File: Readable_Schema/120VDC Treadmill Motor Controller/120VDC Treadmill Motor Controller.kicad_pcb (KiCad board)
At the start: 4 copper layers, 186.8 x 133.2 mm, 141 parts, among them J1 TB005-762-03BE, J2 OSTT7020150, J3 TB0011-350-08BE, J4 TB0011-350-08BE, J5 TB0011-350-08BE, J6 TB0011-350-03BE, J7 OSTT7020150, J9 OSTT7020150, K1 T9GV1L14-24, Q1 IPP200N25N3 G, Q2 IPP200N25N3 G, Q3 IPP200N25N3 G, Q4 IPP200N25N3 G, Q5 IPP60R060P7XKSA1, Q7 DN2450N8-G, Q8 VOM1271T, U1 UCC21530DWKR, U2 UCC21530DWKR, U3 TMCS1126B42QDVGRQ1, U4 SN74HCS08DYYR, U5 TPSI3050QDWZRQ1, U6 AMC1311BDWVR

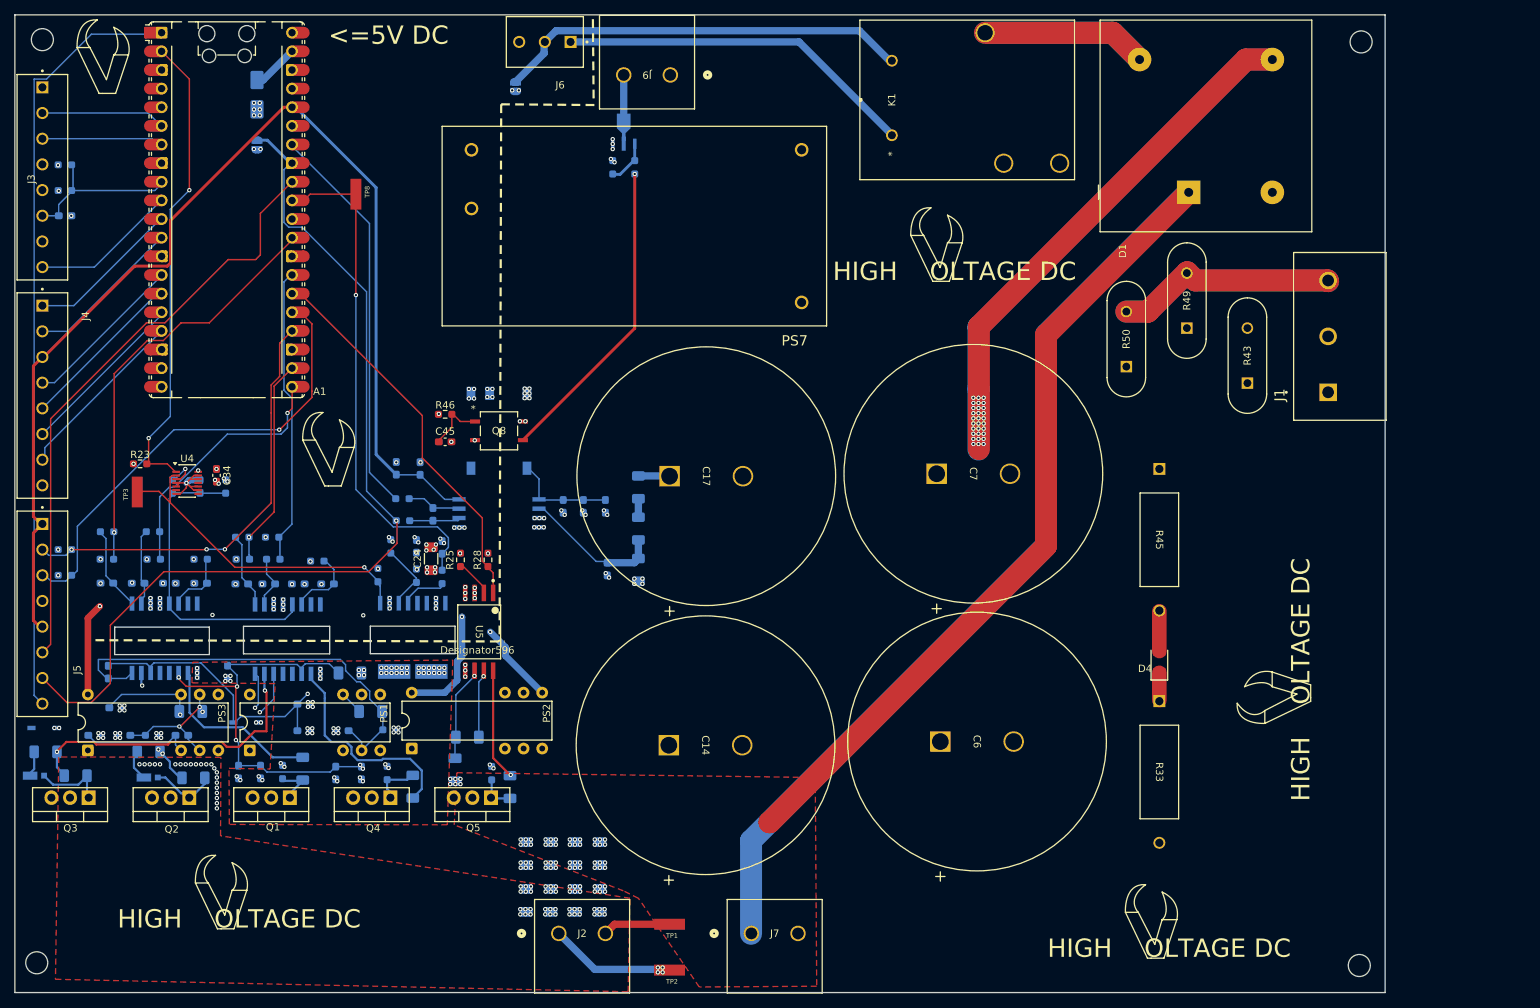
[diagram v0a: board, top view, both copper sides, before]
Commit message: -Finished going back and adding some valuable test points. -Realized that 2oz inner copper layer thickness costs way too much so looking at getting 1oz instead. --Need to double check that my pour sizes and inside traces are sized appropiately for 1oz. Not sure how to check
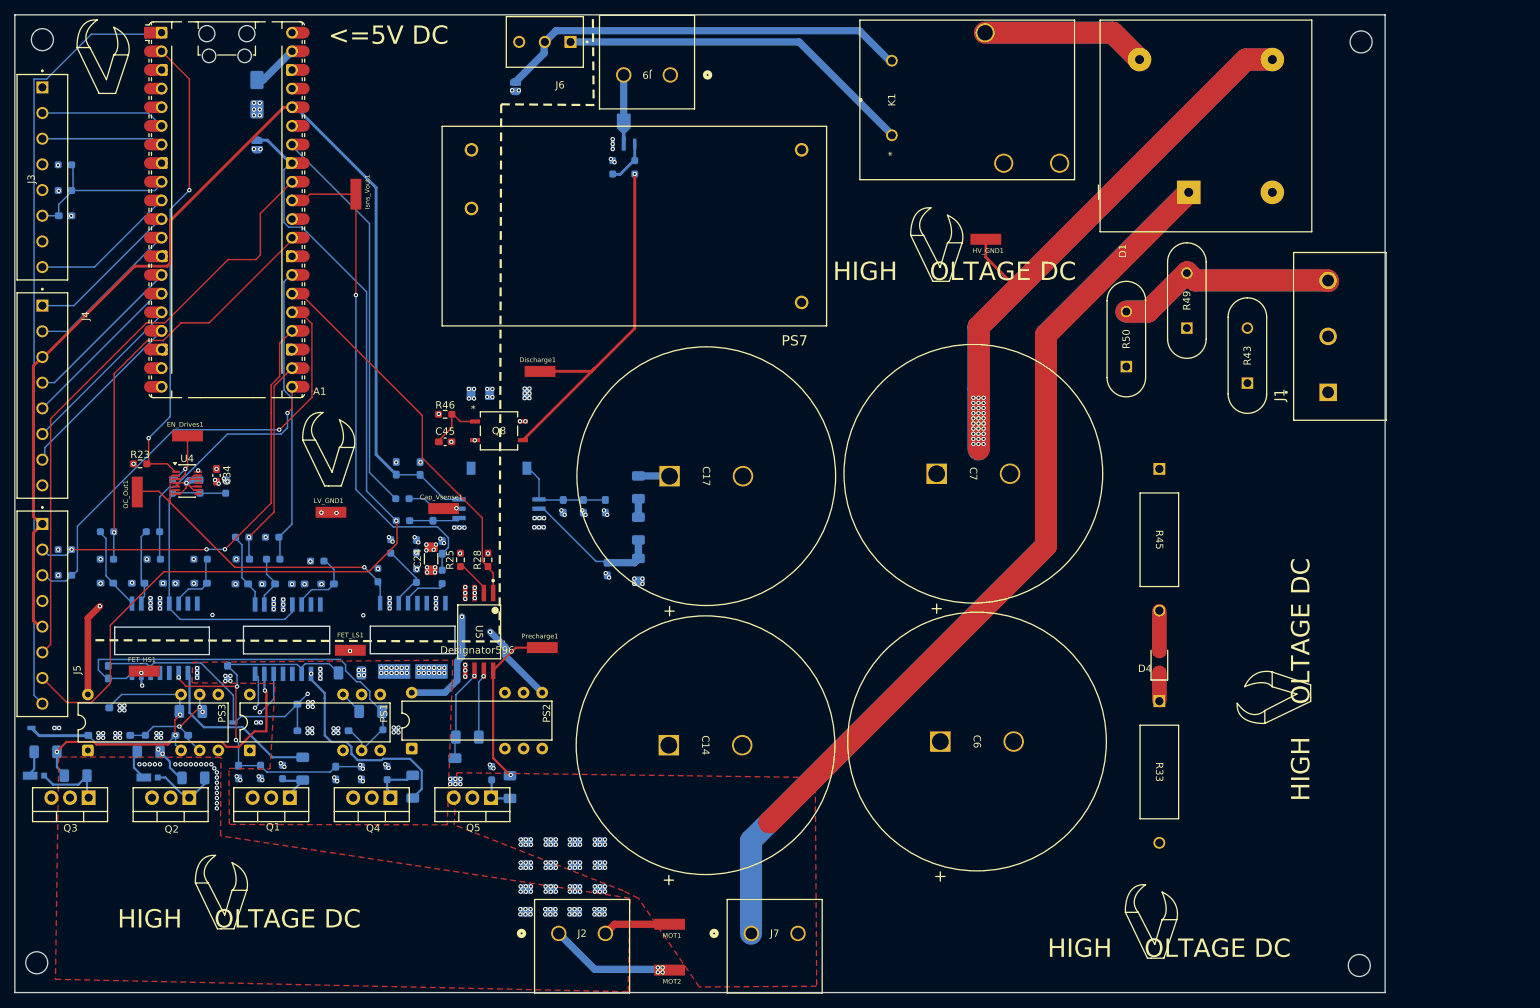
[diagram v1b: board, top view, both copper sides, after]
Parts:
- added Cap_Vsense1: RCWCTE, Treadmill_Feet:RCWCTE, F.Cu at (75.0, 113.1)
- added Discharge1: RCWCTE, Treadmill_Feet:RCWCTE, F.Cu at (88.1, 94.4)
- added EN_Drives1: RCWCTE, Treadmill_Feet:RCWCTE, F.Cu at (40.0, 103.2)
- added FET_HS1: RCWCTE, Treadmill_Feet:RCWCTE, F.Cu at (34.1, 135.2)
- added FET_LS1: RCWCTE, Treadmill_Feet:RCWCTE, F.Cu at (62.2, 132.4)
- added HV_GND1: RCWCTE, Treadmill_Feet:RCWCTE, F.Cu at (148.8, 76.4)
- added LV_GND1: RCWCTE, Treadmill_Feet:RCWCTE, F.Cu at (59.6, 113.6)
- added Precharge1: RCWCTE, Treadmill_Feet:RCWCTE, F.Cu at (88.4, 132.1)
- Q5: value IPP60R060P7XKSA1 -> IPP200N25N3 G
- renumbered TP8 to Isns_Vout1, TP1 to MOT1, TP2 to MOT2, TP3 to OC_Out1
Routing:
- net /H_Bridge/hs_ps_2_-: track 45.0 -> 56.1 mm, vias 2 -> 3
- net HV_GND: track 143.6 -> 152.1 mm
- net Net-(U5-VDRV): track 15.3 -> 23.3 mm
- net Net-(Discharge1-Pad1): track 42.6 -> 50.2 mm
- net Net-(U1-OUTB): track 28.6 -> 35.4 mm, vias 0 -> 2
- net /Feedback/EN_Drives: track 4.30 -> 8.88 mm
- net Net-(U6-VOUTP): vias 0 -> 1
- net Net-(U2-OUTA): vias 3 -> 4
- net LV_GND: vias 64 -> 66

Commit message: -Realizing we can only afford 1oz copper on all 4 layers, trying to rework some of the traces and board fills accordingly. -Moved the smaller caps feeding the top of the H bridge directly in front of the mosfets they're feeding (duh) -Made no effort to reduce crossing signal lines from the gate drives. I think this would probably require a board redesign? -May need to ask the question of whether it may be worth trying to compress thing to reach the next minimum board size
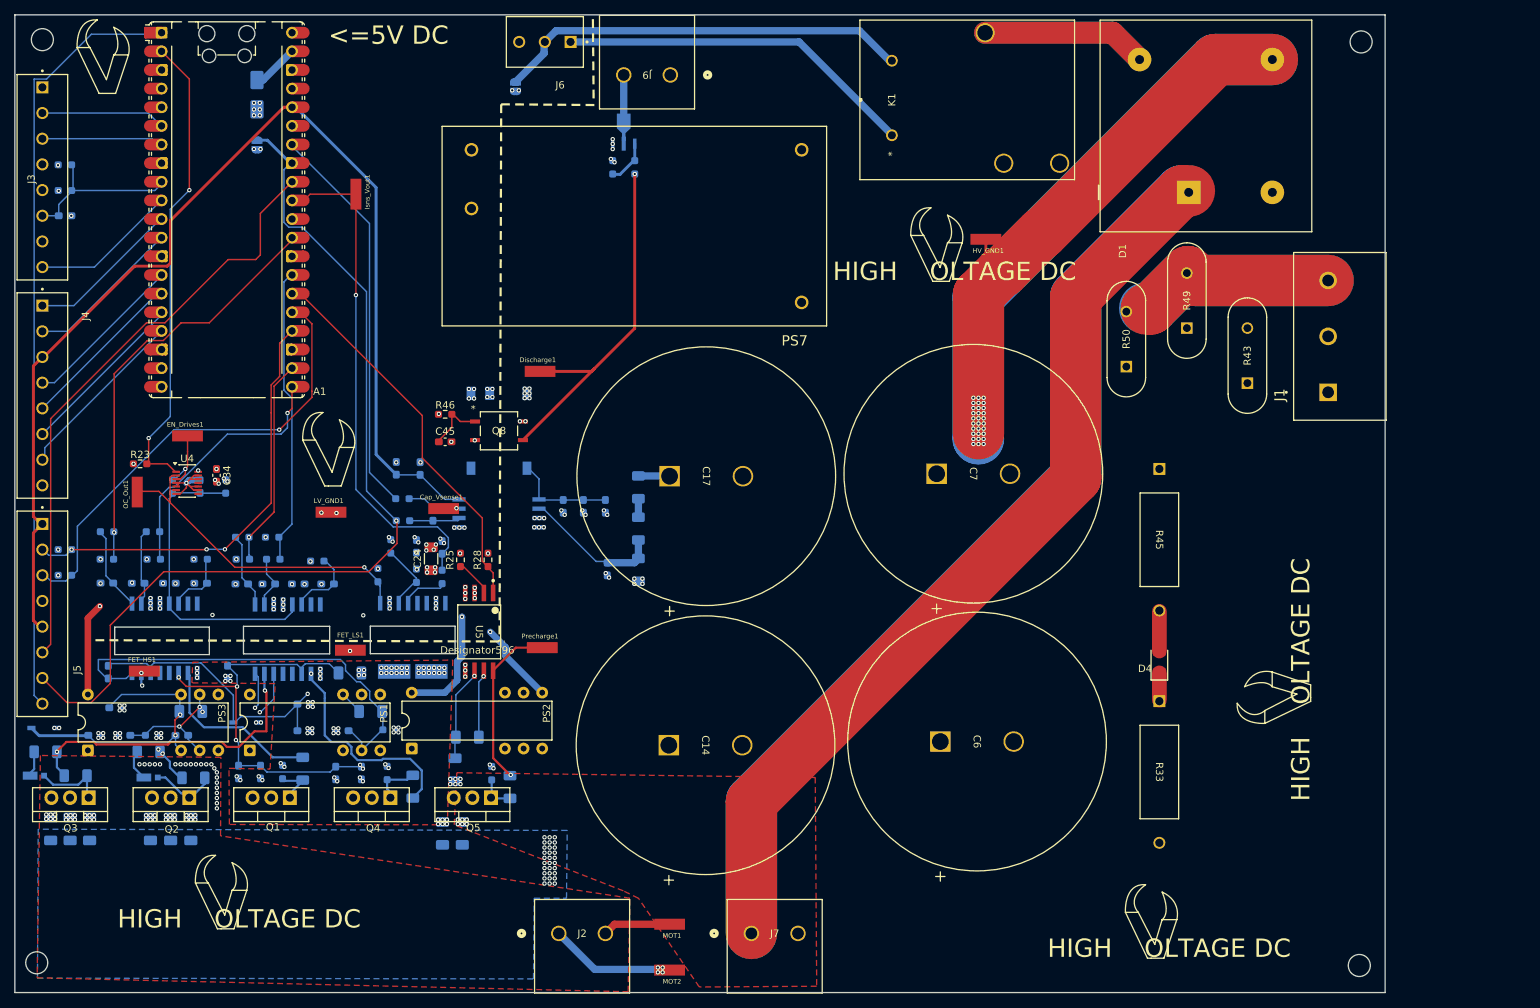
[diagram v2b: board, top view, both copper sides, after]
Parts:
- moved C50 72.9 mm to (24.1, 156.8)
- moved C49 72.2 mm to (21.4, 156.8)
- moved C28 60.3 mm to (26.7, 156.8)
- moved C51 58.6 mm to (37.8, 156.8), turned to -90 degrees
- moved C32 55.4 mm to (35.0, 156.8)
- moved C52 52.5 mm to (40.5, 156.8), turned to -90 degrees
- moved C53 12.4 mm to (77.5, 157.4), turned to -90 degrees
- moved C54 11.7 mm to (74.8, 157.4), turned to -90 degrees
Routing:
- net Net-(D1-+): track 235.3 -> 253.0 mm
- net Net-(J1-Pin_3): track 60.4 -> 55.2 mm
- net HV_GND: track 152.1 -> 153.6 mm, vias 129 -> 111
- added copper zone on B.Cu, net HV_GND

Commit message: For cost reasons we want all 1oz copper layers. This means --Inner copper for 20C rise at 1oz = 33mm min width of either trace or board fills --Outer copper for 20C rise at 1oz = 12mm min width of either trace or board fills
The conjestion near the fets makes this challenging
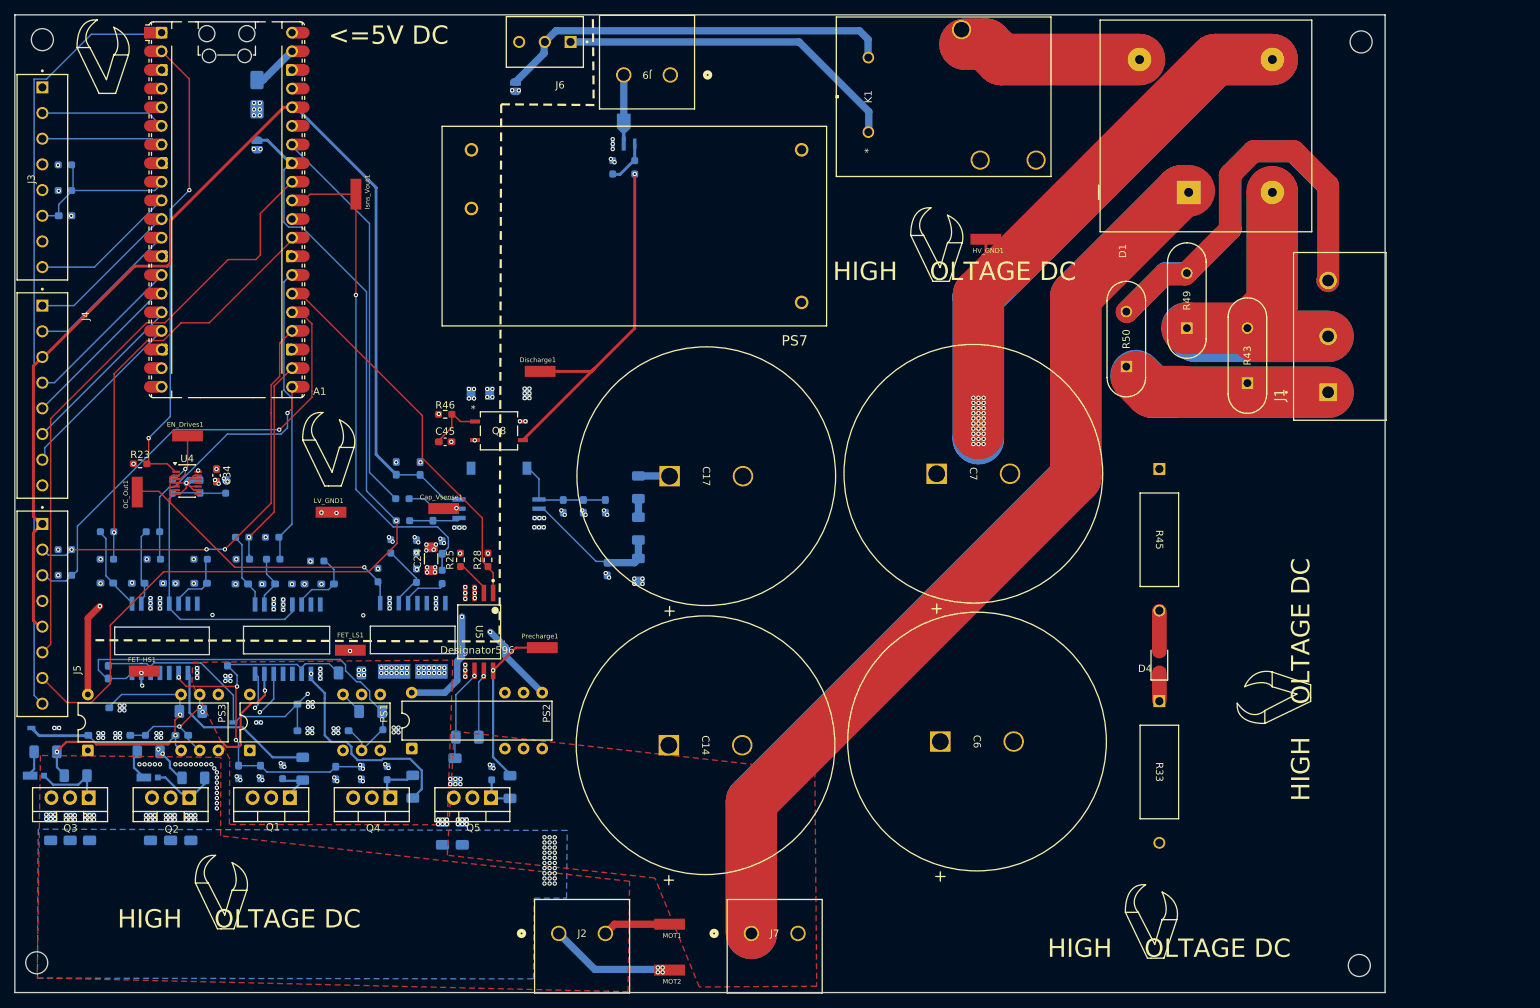
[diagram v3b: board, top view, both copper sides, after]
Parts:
- moved K1 3.24 mm to (132.8, 61.8)
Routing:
- net /Power/N: track 0.00 -> 134.4 mm
- net Net-(J1-Pin_3): track 55.2 -> 111.8 mm
- net /Power/L: track 0.00 -> 54.2 mm
- net Net-(D1-Pad2): track 45.1 -> 49.3 mm
- net Net-(J6-Pin_2): track 56.2 -> 54.2 mm
- net Net-(J6-Pin_1): track 49.1 -> 47.3 mm
- net Net-(U1-OUTA): track 41.9 -> 41.2 mm
- net Net-(U5-VDRV): track 23.3 -> 22.7 mm
- added copper zone on In1.Cu, net /Power/L
- removed copper zone on In1.Cu, net /Power/N

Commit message: -Started to move the Current sense off to the side on the board due to limited space for these massive traces and what not. This entails quite a few random moves
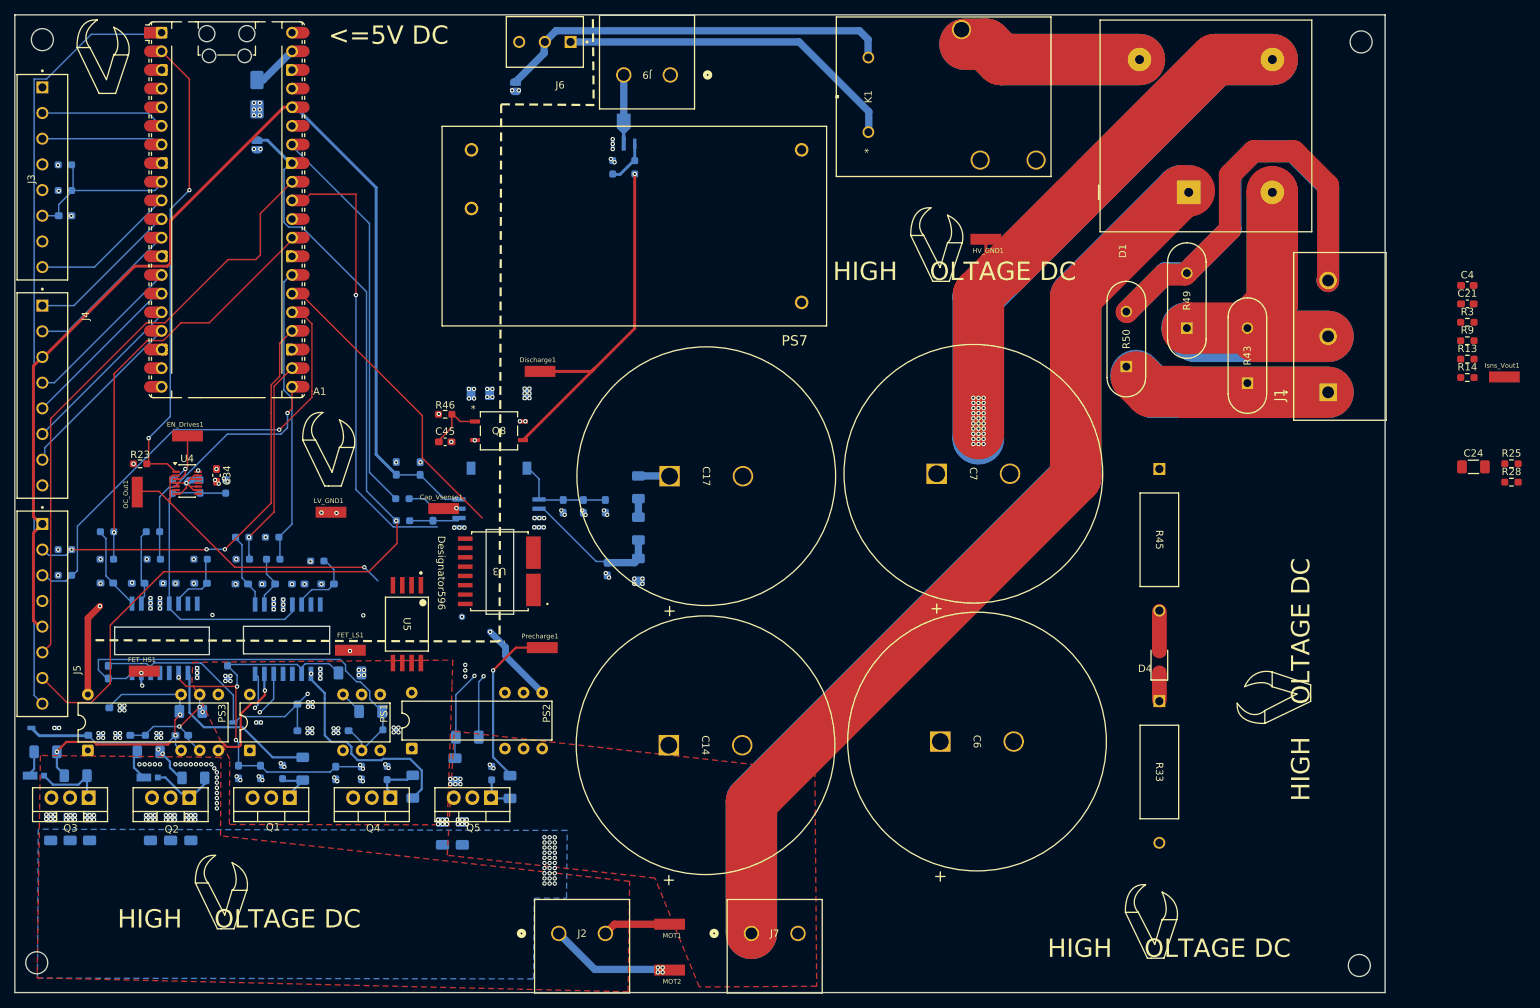
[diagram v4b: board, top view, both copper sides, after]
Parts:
- C21, C4, R13, R14, R3, R9, U3: moved to F.Cu
- moved Isns_Vout1 158.5 mm to (219.5, 95.2), turned to 0 degrees
- moved R9 151.9 mm to (214.5, 90.2), turned to 0 degrees
- moved R3 149.9 mm to (214.5, 87.7), turned to 0 degrees
- moved C21 147.0 mm to (214.5, 85.2), turned to 0 degrees
- moved R13 146.2 mm to (214.5, 92.7), turned to 0 degrees
- moved C4 144.2 mm to (214.5, 82.7), turned to 0 degrees
- moved R25 143.8 mm to (220.5, 107.0), turned to 0 degrees
- moved C24 142.6 mm to (215.3, 107.4), turned to 0 degrees
- moved R14 142.3 mm to (214.5, 95.2), turned to 0 degrees
- moved R28 139.9 mm to (220.5, 109.5), turned to 0 degrees
- moved U3 14.8 mm to (82.5, 121.6), turned to 180 degrees
- moved U5 9.91 mm to (70.0, 128.8)
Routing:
- net /Pi Pico/pre_charge_mcu: track 52.6 -> 42.0 mm
- net Net-(U3-VOC): track 8.88 -> 0.00 mm
- net /Feedback/v_out: track 67.9 -> 61.1 mm
- net Net-(U3-VOUT): track 6.21 -> 0.00 mm
- net Net-(U5-PXFR): track 5.01 -> 0.00 mm
- net /Feedback/OC_out: track 44.4 -> 41.5 mm
- net 5v 15w: track 40.8 -> 41.3 mm, vias 39 -> 26
- net LV_GND: vias 66 -> 48
- net HV_GND: vias 111 -> 99
- net /Feedback/in+: vias 30 -> 18
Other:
- outline, holes or cut-outs redrawn
